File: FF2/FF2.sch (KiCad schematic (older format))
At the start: 77 parts, among them J1 AVR-ISP-6, SW1 RESET, SW2 BOOT, U1 ATmega328P-AU, Y1 16MHz

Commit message: updated footprint for boot and reset headers
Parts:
- SW1, SW2: footprint Connector_PinHeader_1.00mm:PinHeader_1x02_P1.00mm_Vertical -> Connector_PinHeader_1.27mm:PinHeader_1x02_P1.27mm_Vertical
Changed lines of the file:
@@
 F 0 "SW1" H 8050 6335 50  0000 C CNN
 F 1 "RESET" H 8050 6244 50  0000 C CNN
-F 2 "Connector_PinHeader_1.00mm:PinHeader_1x02_P1.00mm_Vertical" H 8050 6250 50  0001 C CNN
+F 2 "Connector_PinHeader_1.27mm:PinHeader_1x02_P1.27mm_Vertical" H 8050 6250 50  0001 C CNN
 F 3 "~" H 8050 6250 50  0001 C CNN
 	1    8050 6050
@@
 F 0 "SW2" H 9300 6335 50  0000 C CNN
 F 1 "BOOT" H 9300 6244 50  0000 C CNN
-F 2 "Connector_PinHeader_1.00mm:PinHeader_1x02_P1.00mm_Vertical" H 9300 6250 50  0001 C CNN
+F 2 "Connector_PinHeader_1.27mm:PinHeader_1x02_P1.27mm_Vertical" H 9300 6250 50  0001 C CNN
 F 3 "~" H 9300 6250 50  0001 C CNN
 	1    9300 6050

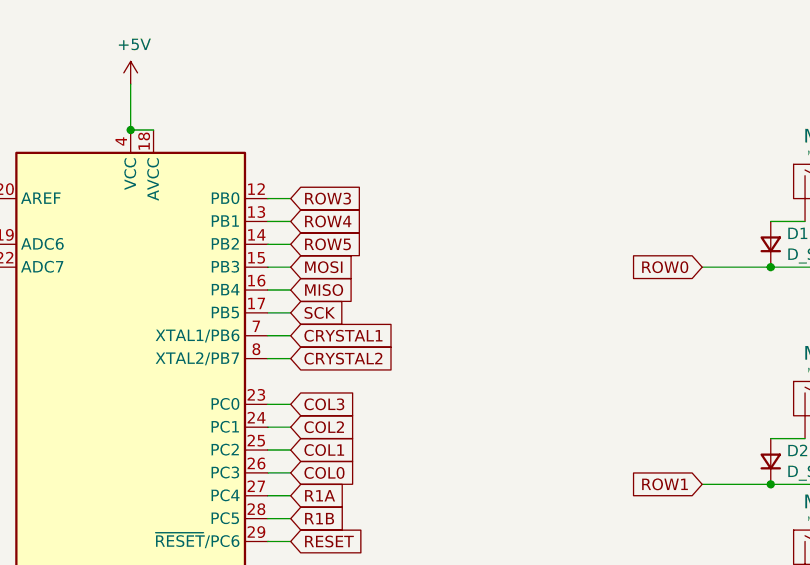
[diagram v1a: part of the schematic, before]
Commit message: added dobber's encoder connection to MCU
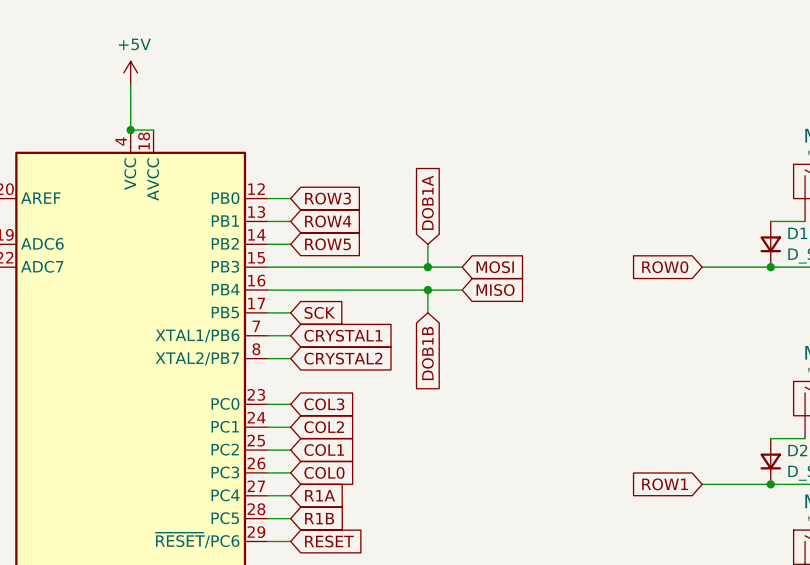
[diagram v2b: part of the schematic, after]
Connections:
- net MISO is gone; now on net DOB1B: J1.1 (MISO), U1.16 (PB4)
- net MOSI is gone; now on net DOB1A: J1.4 (MOSI), U1.15 (PB3)
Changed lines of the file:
@@
 Text GLabel 2550 1700 2    50   Input ~ 0
 SCK
-Text GLabel 2550 1500 2    50   Input ~ 0
+Text GLabel 3300 1500 2    50   Input ~ 0
 MOSI
-Text GLabel 2550 1600 2    50   Input ~ 0
+Text GLabel 3300 1600 2    50   Input ~ 0
 MISO
-Wire Wire Line
-	2550 1600 2450 1600
-Wire Wire Line
-	2550 1500 2450 1500
 Wire Wire Line
 	2550 1700 2450 1700
@@
 Wire Wire Line
 	2450 2500 2550 2500
+Wire Wire Line
+	2450 1500 3150 1500
+Wire Wire Line
+	2450 1600 3150 1600
+Text GLabel 3150 1400 1    50   Input ~ 0
+DOB1A
+Text GLabel 3150 1700 3    50   Input ~ 0
+DOB1B
+Wire Wire Line
+	3150 1700 3150 1600
+Connection ~ 3150 1600
+Wire Wire Line
+	3150 1600 3300 1600
+Wire Wire Line
+	3150 1500 3150 1400
+Connection ~ 3150 1500
+Wire Wire Line
+	3150 1500 3300 1500
 $EndSCHEMATC
